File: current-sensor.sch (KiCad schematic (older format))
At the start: 36 parts, among them J1 ‎0197134001‎, J2 ‎0197134001‎, J3 0731000105, J4 Molex_SL_01x02_Male, J5 Molex_SL_01x02_Male, SW1 PN12SHNA03QE, SW2 OS103011MA7QP1, SW3 OS103011MA7QP1, U1 ACS730xLCTR-20AB, U2 AD8616xRM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

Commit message: add ordering info to schematic
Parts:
- J1, J2: Distributor (none) -> Digikey; Distributor PN (none) -> WM7391-ND; Manufacturer (none) -> Molex; Manufacturer PN (none) -> 0197134001
- J3: Distributor (none) -> Digikey; Distributor PN (none) -> WM5524-ND; Manufacturer (none) -> Molex; Manufacturer PN (none) -> 0731000105
- J4, J5: Distributor (none) -> Digikey; Distributor PN (none) -> WM4800-ND; Manufacturer (none) -> Molex; Manufacturer PN (none) -> 0705430001
- SW1: Distributor (none) -> Digikey; Distributor PN (none) -> CKN1189-ND; Manufacturer (none) -> C&K; Manufacturer PN (none) -> PN12SHNA03QE
- SW2, SW3: Distributor (none) -> Digikey; Distributor PN (none) -> CKN9561-ND; Manufacturer (none) -> C&K; Manufacturer PN (none) -> OS103011MA7QP1
- U1: Distributor (none) -> Digikey; Distributor PN (none) -> 620-1792-1-ND; Manufacturer (none) -> Allegro Microsystems; Manufacturer PN (none) -> ACS730KLCTR-20AB-T
- U2, U3: Distributor (none) -> Digikey; Distributor PN (none) -> AD8616ARZ-REEL7CT-ND; Manufacturer (none) -> Analog Devices; Manufacturer PN (none) -> AD8616ARZ-REEL7
- U4: Distributor (none) -> Digikey; Distributor PN (none) -> NCP718ASN500T1GOSCT-ND; Manufacturer (none) -> ON Semi; Manufacturer PN (none) -> NCP718ASN500T1G
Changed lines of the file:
@@
 F 2 "Package_SO:SOIC-8_3.9x4.9mm_P1.27mm" H 8150 4650 50  0001 C CNN
 F 3 "https://www.analog.com/media/en/technical-documentation/data-sheets/AD8615_8616_8618.pdf" H 8300 4800 50  0001 C CNN
+F 4 "Digikey" H 8050 4650 50  0001 C CNN "Distributor"
+F 5 "AD8616ARZ-REEL7CT-ND" H 8050 4650 50  0001 C CNN "Distributor PN"
+F 6 "Analog Devices" H 8050 4650 50  0001 C CNN "Manufacturer"
+F 7 "AD8616ARZ-REEL7" H 8050 4650 50  0001 C CNN "Manufacturer PN"
 	1    8050 4650
 	1    0    0    -1
@@
 F 2 "Package_SO:SOIC-8_3.9x4.9mm_P1.27mm" H 7100 4550 50  0001 C CNN
 F 3 "https://www.analog.com/media/en/technical-documentation/data-sheets/AD8615_8616_8618.pdf" H 7250 4700 50  0001 C CNN
+F 4 "Digikey" H 7000 4550 50  0001 C CNN "Distributor"
+F 5 "AD8616ARZ-REEL7CT-ND" H 7000 4550 50  0001 C CNN "Distributor PN"
+F 6 "Analog Devices" H 7000 4550 50  0001 C CNN "Manufacturer"
+F 7 "AD8616ARZ-REEL7" H 7000 4550 50  0001 C CNN "Manufacturer PN"
 	2    7000 4550
 	1    0    0    1
@@
 F 2 "Package_SO:SOIC-8_3.9x4.9mm_P1.27mm" H 5300 4450 50  0001 C CNN
 F 3 "https://www.analog.com/media/en/technical-documentation/data-sheets/AD8615_8616_8618.pdf" H 5450 4600 50  0001 C CNN
+F 4 "Digikey" H 5200 4450 50  0001 C CNN "Distributor"
+F 5 "AD8616ARZ-REEL7CT-ND" H 5200 4450 50  0001 C CNN "Distributor PN"
+F 6 "Analog Devices" H 5200 4450 50  0001 C CNN "Manufacturer"
+F 7 "AD8616ARZ-REEL7" H 5200 4450 50  0001 C CNN "Manufacturer PN"
 	1    5200 4450
 	1    0    0    1
@@
 F 2 "Package_SO:SOIC-8_3.9x4.9mm_P1.27mm" H 4400 5950 50  0001 C CNN
 F 3 "https://www.analog.com/media/en/technical-documentation/data-sheets/AD8615_8616_8618.pdf" H 4550 6100 50  0001 C CNN
+F 4 "Digikey" H 4300 5950 50  0001 C CNN "Distributor"
+F 5 "AD8616ARZ-REEL7CT-ND" H 4300 5950 50  0001 C CNN "Distributor PN"
+F 6 "Analog Devices" H 4300 5950 50  0001 C CNN "Manufacturer"
+F 7 "AD8616ARZ-REEL7" H 4300 5950 50  0001 C CNN "Manufacturer PN"
 	2    4300 5950
 	1    0    0    -1
@@
 F 2 "Package_SO:SOIC-8_3.9x4.9mm_P1.27mm" H 5200 4450 50  0001 C CNN
 F 3 "https://www.analog.com/media/en/technical-documentation/data-sheets/AD8615_8616_8618.pdf" H 5350 4600 50  0001 C CNN
+F 4 "Digikey" H 5100 4450 50  0001 C CNN "Distributor"
+F 5 "AD8616ARZ-REEL7CT-ND" H 5100 4450 50  0001 C CNN "Distributor PN"
+F 6 "Analog Devices" H 5100 4450 50  0001 C CNN "Manufacturer"
+F 7 "AD8616ARZ-REEL7" H 5100 4450 50  0001 C CNN "Manufacturer PN"
 	3    5100 4450
 	1    0    0    -1
@@
 F 2 "Package_SO:SOIC-8_3.9x4.9mm_P1.27mm" H 4300 5950 50  0001 C CNN
 F 3 "https://www.analog.com/media/en/technical-documentation/data-sheets/AD8615_8616_8618.pdf" H 4450 6100 50  0001 C CNN
+F 4 "Digikey" H 4200 5950 50  0001 C CNN "Distributor"
+F 5 "AD8616ARZ-REEL7CT-ND" H 4200 5950 50  0001 C CNN "Distributor PN"
+F 6 "Analog Devices" H 4200 5950 50  0001 C CNN "Manufacturer"
+F 7 "AD8616ARZ-REEL7" H 4200 5950 50  0001 C CNN "Manufacturer PN"
 	3    4200 5950
 	1    0    0    -1
@@
 F 2 "Package_TO_SOT_SMD:TSOT-23-5" H 5450 1900 50  0001 C CNN
 F 3 "https://www.onsemi.com/pub/Collateral/NCP718-D.PDF" H 5450 1600 50  0001 C CNN
+F 4 "Digikey" H 5450 1500 50  0001 C CNN "Distributor"
+F 5 "NCP718ASN500T1GOSCT-ND" H 5450 1500 50  0001 C CNN "Distributor PN"
+F 6 "ON Semi" H 5450 1500 50  0001 C CNN "Manufacturer"
+F 7 "NCP718ASN500T1G" H 5450 1500 50  0001 C CNN "Manufacturer PN"
 	1    5450 1500
 	1    0    0    -1
@@
 F 2 "Connector_Coaxial_gkeeth:BNC_Molex_73100-0105_Horizontal" H 9350 4650 50  0001 C CNN
 F 3 " ~" H 9350 4650 50  0001 C CNN
+F 4 "Digikey" H 9350 4650 50  0001 C CNN "Distributor"
+F 5 "WM5524-ND" H 9350 4650 50  0001 C CNN "Distributor PN"
+F 6 "Molex" H 9350 4650 50  0001 C CNN "Manufacturer"
+F 7 "0731000105" H 9350 4650 50  0001 C CNN "Manufacturer PN"
 	1    9350 4650
 	1    0    0    -1
@@
 F 2 "Connector_Molex_Quixon:Connector_Molex_Quixon_19713-4001_1x01_Horizontal" H 1250 4250 50  0001 C CNN
 F 3 "~" H 1250 4250 50  0001 C CNN
+F 4 "Digikey" H 1250 4250 50  0001 C CNN "Distributor"
+F 5 "WM7391-ND" H 1250 4250 50  0001 C CNN "Distributor PN"
+F 6 "Molex" H 1250 4250 50  0001 C CNN "Manufacturer"
+F 7 "0197134001" H 1250 4250 50  0001 C CNN "Manufacturer PN"
 	1    1250 4250
 	1    0    0    -1
@@
 F 2 "Connector_Molex_Quixon:Connector_Molex_Quixon_19713-4001_1x01_Horizontal" H 1250 4450 50  0001 C CNN
 F 3 "~" H 1250 4450 50  0001 C CNN
+F 4 "Digikey" H 1250 4450 50  0001 C CNN "Distributor"
+F 5 "WM7391-ND" H 1250 4450 50  0001 C CNN "Distributor PN"
+F 6 "Molex" H 1250 4450 50  0001 C CNN "Manufacturer"
+F 7 "0197134001" H 1250 4450 50  0001 C CNN "Manufacturer PN"
 	1    1250 4450
 	1    0    0    -1
@@
 F 2 "Button_Switch_THT_gkeeth:SW_Push_SPDT_CK_PN1xSxxx03QE" H 3850 1200 50  0001 C CNN
 F 3 "https://www.ckswitches.com/media/1413/pn.pdf" H 3850 1200 50  0001 C CNN
+F 4 "Digikey" H 3850 1200 50  0001 C CNN "Distributor"
+F 5 "CKN1189-ND" H 3850 1200 50  0001 C CNN "Distributor PN"
+F 6 "C&K" H 3850 1200 50  0001 C CNN "Manufacturer"
+F 7 "PN12SHNA03QE" H 3850 1200 50  0001 C CNN "Manufacturer PN"
 	1    3850 1200
 	1    0    0    -1
@@
 F 2 "Button_Switch_THT_gkeeth:SW_Slide_SP3T_CK_OS103011MA7QP1" H 6175 3525 50  0001 C CNN
 F 3 "https://www.ckswitches.com/media/1428/os.pdf" H 6175 3525 50  0001 C CNN
+F 4 "Digikey" H 6800 3350 50  0001 C CNN "Distributor"
+F 5 "CKN9561-ND" H 6800 3350 50  0001 C CNN "Distributor PN"
+F 6 "C&K" H 6800 3350 50  0001 C CNN "Manufacturer"
+F 7 "OS103011MA7QP1" H 6800 3350 50  0001 C CNN "Manufacturer PN"
 	1    6800 3350
 	1    0    0    -1
@@
 F 2 "Connector_Molex_SL:Molex_SL_A-70543-0001_1x02_P2.54mm_Vertical" H 7500 1600 50  0001 C CNN
 F 3 "https://www.molex.com/pdm_docs/sd/705430001_sd.pdf" H 7500 1600 50  0001 C CNN
+F 4 "Digikey" H 7500 1600 50  0001 C CNN "Distributor"
+F 5 "WM4800-ND" H 7500 1600 50  0001 C CNN "Distributor PN"
+F 6 "Molex" H 7500 1600 50  0001 C CNN "Manufacturer"
+F 7 "0705430001" H 7500 1600 50  0001 C CNN "Manufacturer PN"
 	1    7500 1600
 	-1   0    0    -1
@@
 F 2 "Button_Switch_THT_gkeeth:SW_Slide_SP3T_CK_OS103011MA7QP1" H 4225 3525 50  0001 C CNN
 F 3 "https://www.ckswitches.com/media/1428/os.pdf" H 4225 3525 50  0001 C CNN
+F 4 "Digikey" H 4850 3350 50  0001 C CNN "Distributor"
+F 5 "CKN9561-ND" H 4850 3350 50  0001 C CNN "Distributor PN"
+F 6 "C&K" H 4850 3350 50  0001 C CNN "Manufacturer"
+F 7 "OS103011MA7QP1" H 4850 3350 50  0001 C CNN "Manufacturer PN"
 	1    4850 3350
 	1    0    0    -1
@@
 F 2 "Connector_Molex_SL:Molex_SL_A-70543-0001_1x02_P2.54mm_Vertical" H 2150 1200 50  0001 C CNN
 F 3 "https://www.molex.com/pdm_docs/sd/705430001_sd.pdf" H 2150 1200 50  0001 C CNN
+F 4 "Digikey" H 2150 1200 50  0001 C CNN "Distributor"
+F 5 "WM4800-ND" H 2150 1200 50  0001 C CNN "Distributor PN"
+F 6 "Molex" H 2150 1200 50  0001 C CNN "Manufacturer"
+F 7 "0705430001" H 2150 1200 50  0001 C CNN "Manufacturer PN"
 	1    2150 1200
 	1    0    0    -1
@@
 F 2 "Package_SO:SOIC-8_3.9x4.9mm_P1.27mm" H 2950 4250 50  0001 L CIN
 F 3 "http://www.allegromicro.com/~/media/Files/Datasheets/ACS730-Datasheet.ashx?la=en" H 2600 4350 50  0001 C CNN
+F 4 "Digikey" H 2600 4350 50  0001 C CNN "Distributor"
+F 5 "620-1792-1-ND" H 2600 4350 50  0001 C CNN "Distributor PN"
+F 6 "Allegro Microsystems" H 2600 4350 50  0001 C CNN "Manufacturer"
+F 7 "ACS730KLCTR-20AB-T" H 2600 4350 50  0001 C CNN "Manufacturer PN"
 	1    2600 4350
 	1    0    0    -1

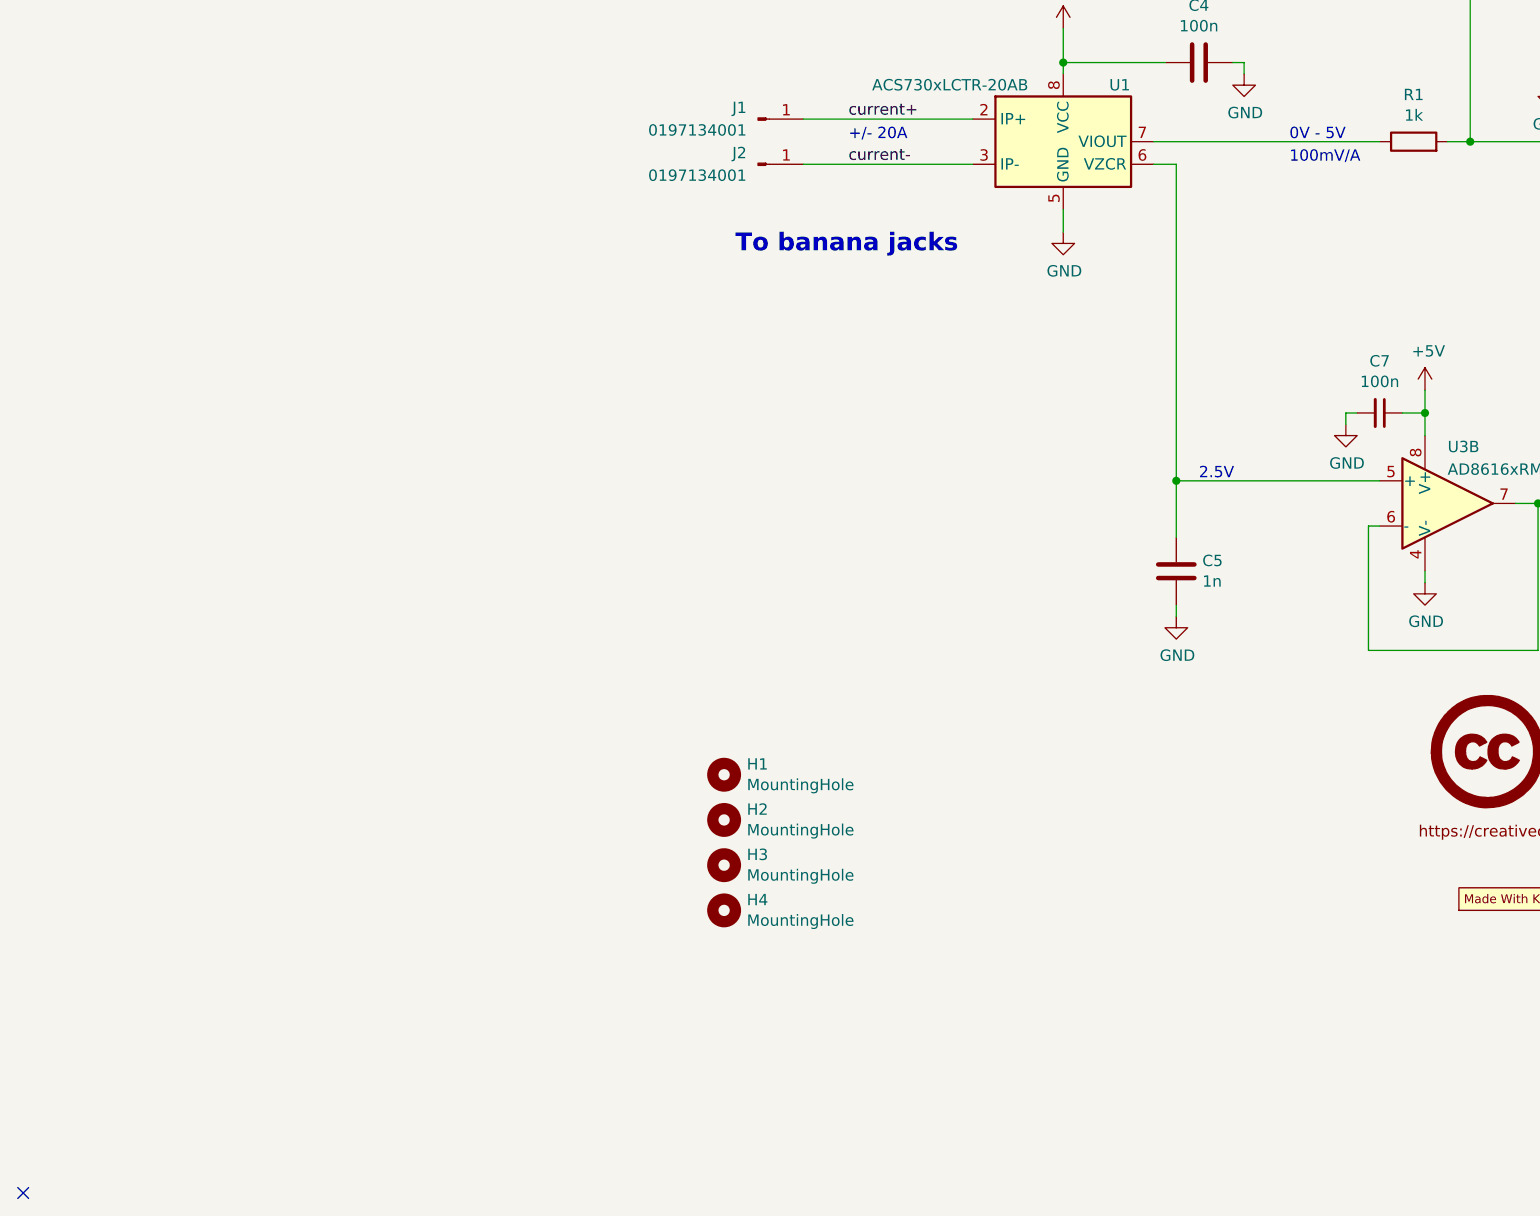
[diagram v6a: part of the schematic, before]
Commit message: add zero-current offset trim
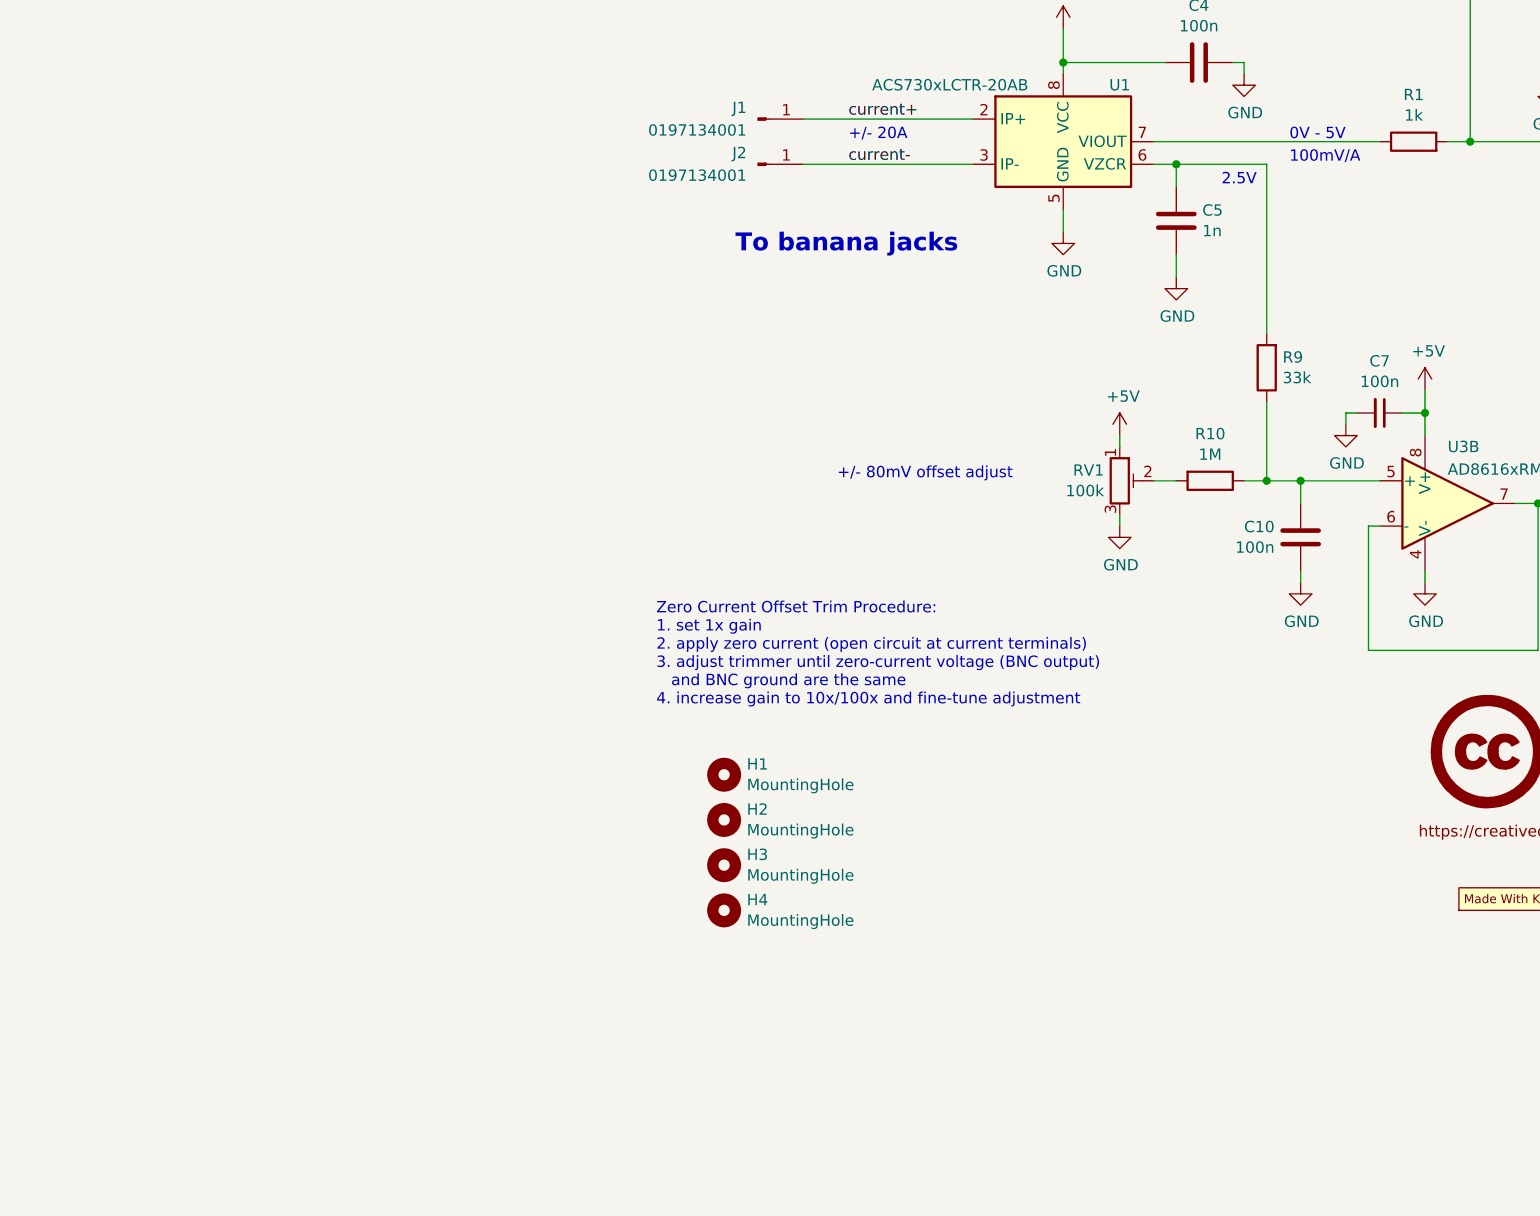
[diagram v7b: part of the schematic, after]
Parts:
- added C10: 100n, Capacitor_SMD:C_0603_1608Metric, symbol Device:C
- added R10: 1M, Resistor_SMD:R_0603_1608Metric, symbol Device:R
- added R9: 33k, Resistor_SMD:R_0603_1608Metric, symbol Device:R
- added RV1: 100k, Potentiometer_SMD:Potentiometer_Vishay_TS53YL_Vertical, symbol Device:R_POT_TRIM
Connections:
- net +5V: now also RV1.1
- net GND: now also C10.2, RV1.3
- net at C5.1, U1.6 (VZCR): now also R9.2; no longer U3.5 (+)
- new net: C10.1, R10.1, R9.1, U3.5 (+)
- new net: R10.2, RV1.2
- no-connect marks 3 -> 2
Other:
- note added: "+/- 80mV offset adjust"
- note added: "Zero Current Offset Trim Procedure:\n1. set 1x gain\n2. apply zero current (open circuit at current terminals)\n3. adjust trimmer until zero-current voltage (BNC output)\n and BNC ground are the same\n4. increase gain to 10x/100x and fine-tune adjustment"
- moved on the sheet: C5
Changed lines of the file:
@@
 Sheet 1 1
 Title "Current Sensor"
-Date "2020-12-07"
-Rev "1"
+Date "2021-01-03"
+Rev "2"
 Comp "G. Keeth"
 Comment1 ""
@@
 L Device:C C5
 U 1 1 5EFC8D89
-P 3100 6250
-F 0 "C5" H 3215 6296 50  0000 L CNN
-F 1 "1n" H 3215 6205 50  0000 L CNN
-F 2 "Capacitor_SMD:C_0603_1608Metric" H 3138 6100 50  0001 C CNN
-F 3 "~" H 3100 6250 50  0001 C CNN
-	1    3100 6250
+P 3100 4700
+F 0 "C5" H 3215 4746 50  0000 L CNN
+F 1 "1n" H 3215 4655 50  0000 L CNN
+F 2 "Capacitor_SMD:C_0603_1608Metric" H 3138 4550 50  0001 C CNN
+F 3 "~" H 3100 4700 50  0001 C CNN
+	1    3100 4700
 	1    0    0    -1
 $EndComp
@@
 L power:GND #PWR0105
 U 1 1 5EFC981E
-P 3100 6450
-F 0 "#PWR0105" H 3100 6200 50  0001 C CNN
-F 1 "GND" H 3105 6277 50  0000 C CNN
-F 2 "" H 3100 6450 50  0001 C CNN
-F 3 "" H 3100 6450 50  0001 C CNN
-	1    3100 6450
-	1    0    0    -1
-$EndComp
-Wire Wire Line
-	3100 6400 3100 6450
+P 3100 4950
+F 0 "#PWR0105" H 3100 4700 50  0001 C CNN
+F 1 "GND" H 3105 4777 50  0000 C CNN
+F 2 "" H 3100 4950 50  0001 C CNN
+F 3 "" H 3100 4950 50  0001 C CNN
+	1    3100 4950
+	1    0    0    -1
+$EndComp
+Wire Wire Line
+	3100 4850 3100 4950
 $Comp
 L Device:C C4
@@
 Wire Wire Line
 	3000 4450 3100 4450
-Text Notes 3200 5850 0    50   ~ 0
+Text Notes 3300 4550 0    50   ~ 0
 2.5V
 Text Notes 3600 4350 0    50   ~ 0
@@
 	4000 4350 3000 4350
 Wire Wire Line
-	3100 4450 3100 5850
-Wire Wire Line
-	4000 5850 3100 5850
-Connection ~ 3100 5850
-Wire Wire Line
-	3100 5850 3100 6100
-Wire Wire Line
 	5900 4450 5800 4450
 Connection ~ 5800 4450
@@
 	1    0    0    -1
 $EndComp
-NoConn ~ -2000 9000
 $Comp
 L power:PWR_FLAG #FLG0102
@@
 Text Notes 9450 4900 0    50   ~ 0
 gain x 100mV/A
+$Comp
+L Device:R_POT_TRIM RV1
+U 1 1 5FF299EA
+P 2850 5850
+F 0 "RV1" H 2781 5896 50  0000 R CNN
+F 1 "100k" H 2781 5805 50  0000 R CNN
+F 2 "Potentiometer_SMD:Potentiometer_Vishay_TS53YL_Vertical" H 2850 5850 50  0001 C CNN
+F 3 "~" H 2850 5850 50  0001 C CNN
+F 4 "Vishay Svernice" H 2850 5850 50  0001 C CNN "Manufacturer"
+F 5 "TS53YL104MR10" H 2850 5850 50  0001 C CNN "Manufacturer PN"
+	1    2850 5850
+	1    0    0    -1
+$EndComp
+$Comp
+L power:GND #PWR0119
+U 1 1 5FF2A0C5
+P 2850 6050
+F 0 "#PWR0119" H 2850 5800 50  0001 C CNN
+F 1 "GND" H 2855 5877 50  0000 C CNN
+F 2 "" H 2850 6050 50  0001 C CNN
+F 3 "" H 2850 6050 50  0001 C CNN
+	1    2850 6050
+	1    0    0    -1
+$EndComp
+$Comp
+L power:+5V #PWR0120
+U 1 1 5FF2A4DA
+P 2850 5650
+F 0 "#PWR0120" H 2850 5500 50  0001 C CNN
+F 1 "+5V" H 2865 5823 50  0000 C CNN
+F 2 "" H 2850 5650 50  0001 C CNN
+F 3 "" H 2850 5650 50  0001 C CNN
+	1    2850 5650
+	1    0    0    -1
+$EndComp
+$Comp
+L Device:R R10
+U 1 1 5FF35394
+P 3250 5850
+F 0 "R10" V 3043 5850 50  0000 C CNN
+F 1 "1M" V 3134 5850 50  0000 C CNN
+F 2 "Resistor_SMD:R_0603_1608Metric" V 3180 5850 50  0001 C CNN
+F 3 "~" H 3250 5850 50  0001 C CNN
+	1    3250 5850
+	0    1    1    0
+$EndComp
+Wire Wire Line
+	3000 5850 3100 5850
+$Comp
+L Device:R R9
+U 1 1 5FF44480
+P 3500 5350
+F 0 "R9" H 3430 5304 50  0000 R CNN
+F 1 "33k" H 3430 5395 50  0000 R CNN
+F 2 "Resistor_SMD:R_0603_1608Metric" V 3430 5350 50  0001 C CNN
+F 3 "~" H 3500 5350 50  0001 C CNN
+	1    3500 5350
+	-1   0    0    1
+$EndComp
+Wire Wire Line
+	3100 4450 3500 4450
+Wire Wire Line
+	3500 4450 3500 5200
+Connection ~ 3100 4450
+Wire Wire Line
+	3100 4450 3100 4550
+Wire Wire Line
+	3400 5850 3500 5850
+Wire Wire Line
+	3500 5850 3500 5500
+Wire Wire Line
+	3500 5850 3650 5850
+Connection ~ 3500 5850
+Text Notes 800  6850 0    50   ~ 0
+Zero Current Offset Trim Procedure:\n1. set 1x gain\n2. apply zero current (open circuit at current terminals)\n3. adjust trimmer until zero-current voltage (BNC output)\n   and BNC ground are the same\n4. increase gain to 10x/100x and fine-tune adjustment
+Text Notes 1600 5850 0    50   ~ 0
++/- 80mV offset adjust
+Wire Wire Line
+	2850 5700 2850 5650
+Wire Wire Line
+	2850 6000 2850 6050
+$Comp
+L Device:C C10
+U 1 1 5FFA0B84
+P 3650 6100
+F 0 "C10" H 3535 6146 50  0000 R CNN
+F 1 "100n" H 3535 6055 50  0000 R CNN
+F 2 "Capacitor_SMD:C_0603_1608Metric" H 3688 5950 50  0001 C CNN
+F 3 "~" H 3650 6100 50  0001 C CNN
+	1    3650 6100
+	1    0    0    -1
+$EndComp
+$Comp
+L power:GND #PWR01
+U 1 1 5FFA1B93
+P 3650 6300
+F 0 "#PWR01" H 3650 6050 50  0001 C CNN
+F 1 "GND" H 3655 6127 50  0000 C CNN
+F 2 "" H 3650 6300 50  0001 C CNN
+F 3 "" H 3650 6300 50  0001 C CNN
+	1    3650 6300
+	1    0    0    -1
+$EndComp
+Wire Wire Line
+	3650 6300 3650 6250
+Wire Wire Line
+	3650 5950 3650 5850
+Connection ~ 3650 5850
+Wire Wire Line
+	3650 5850 4000 5850
 $EndSCHEMATC
